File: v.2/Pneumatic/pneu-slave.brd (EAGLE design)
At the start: 30.5 x 50.8 mm, 42 parts, among them IC3 ATMEGA328, Q1 16Mhz, U2 NCP1117-5

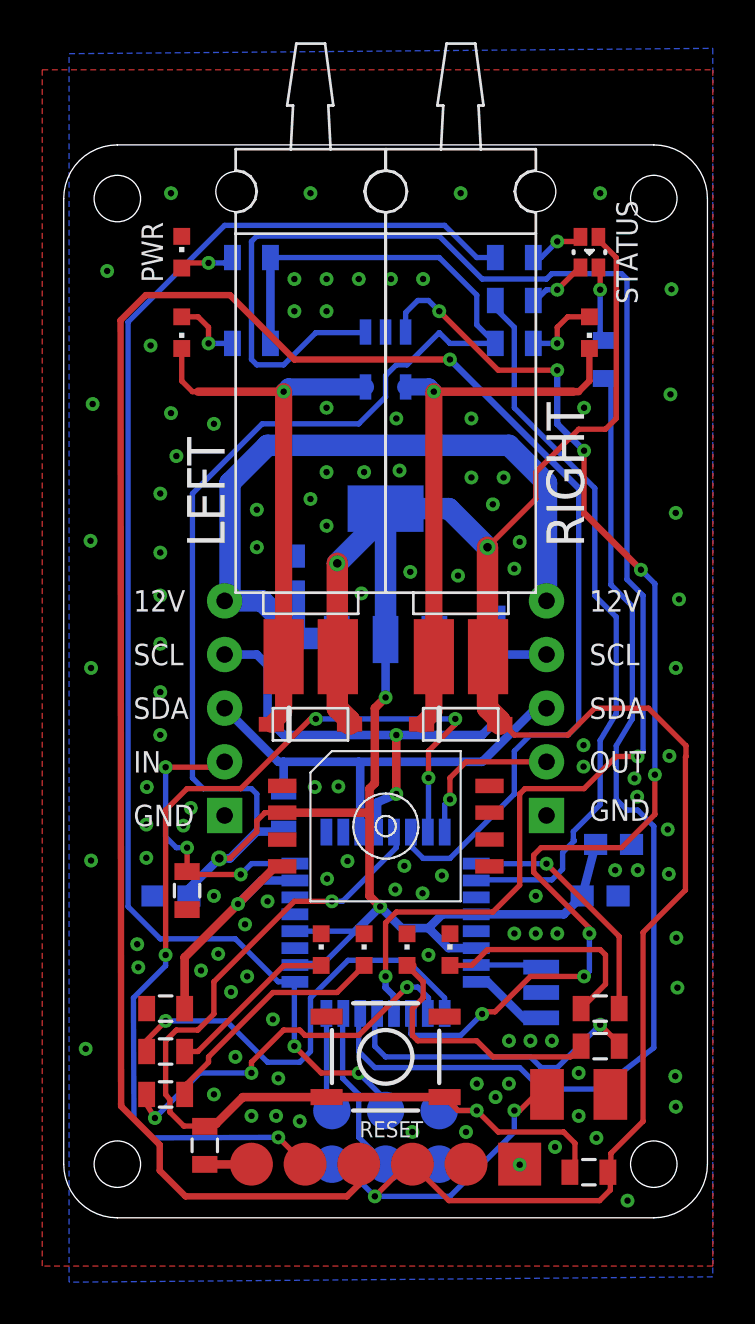
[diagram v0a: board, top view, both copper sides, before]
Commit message: minor changes
getting ready for production:

correct indicator led position on master board
add corner drills to slave boards
generate silk screens
adjust edge connector distance for better fit
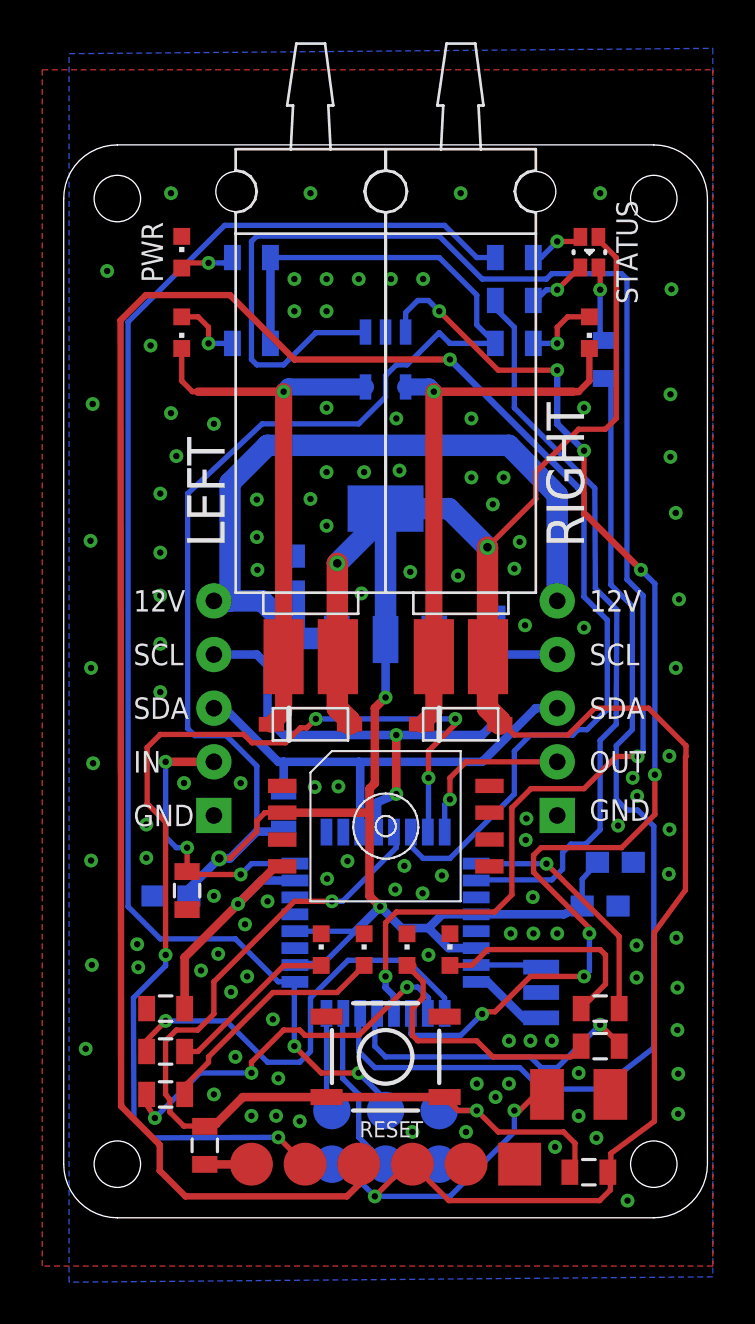
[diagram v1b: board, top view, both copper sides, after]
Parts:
- moved C10 0.85 mm to (23.6, 16.8)
- moved U$24 0.51 mm to (4.57, 24.1)
- moved U$23 0.51 mm to (20.8, 24.1)
- moved C8 0.48 mm to (22.9, 14.8)
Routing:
- net TX: track 45.7 -> 49.0 mm
- net RX: track 101.9 -> 103.4 mm
- net SCL: track 27.2 -> 28.2 mm
- net SDA: track 22.1 -> 23.1 mm
- net VIN: track 35.8 -> 36.5 mm
- net +5V: track 218.9 -> 218.3 mm
- net D2/OUT: track 7.56 -> 8.06 mm
- net GND: vias 112 -> 117

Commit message: small updates..
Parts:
- removed C3: 22uF, rcl:SMC_B
- removed U$1: MPXHZ6400, digikey:MPXHZ6400
- added C4: 22uF, SparkFun-Capacitors:1206
- added U1: NCP1117-5, SmartPrj:LINEAR_SOT223
- C5: device SparkFun-Capacitors:0805 -> SparkFun-Capacitors:0603-CAP
- LED_PR1, LED_PR2, LED_PR3, LED_PR4, LED_V1, LED_V2: value (none) -> WHITE
- LED_PWR: value (none) -> RED
- U2: value NCP1117-5 -> MPXHZ6400; device SmartPrj:LINEAR_SOT223 -> digikey:MPXHZ6400
- moved U2 11.9 mm to (12.7, 18.5), flipped to the top
- renumbered 1 to LED_PR4, 2 to LED_V2, 3 to LED_V1, 5 to LED_PR3, 7 to LED_PR1, 8 to LED_PR2, IC3 to U0, PWR to LED_PWR, U$21 to LED_STATUS, U$3 to U3
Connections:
- net +5V: now also C4.1, U1.2, U1.4; no longer C3.+, U$1.2, U2.4
- net A0/PRESSURE: now also U2.4; no longer U$1.4
- net GND: now also C4.2, U1.1, U2.3; no longer C3.-, U$1.3, U2.1
- net VIN: now also U1.3; no longer U2.3
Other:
- board text added: "PWR"
- board text added: "STAT"
- board text removed: "STATUS"
